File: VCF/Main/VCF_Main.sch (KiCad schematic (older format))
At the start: 56 parts, among them J1 Power, J2 Power, U1 TL072, U2 TL072, U3 AS3320, U4 TL072

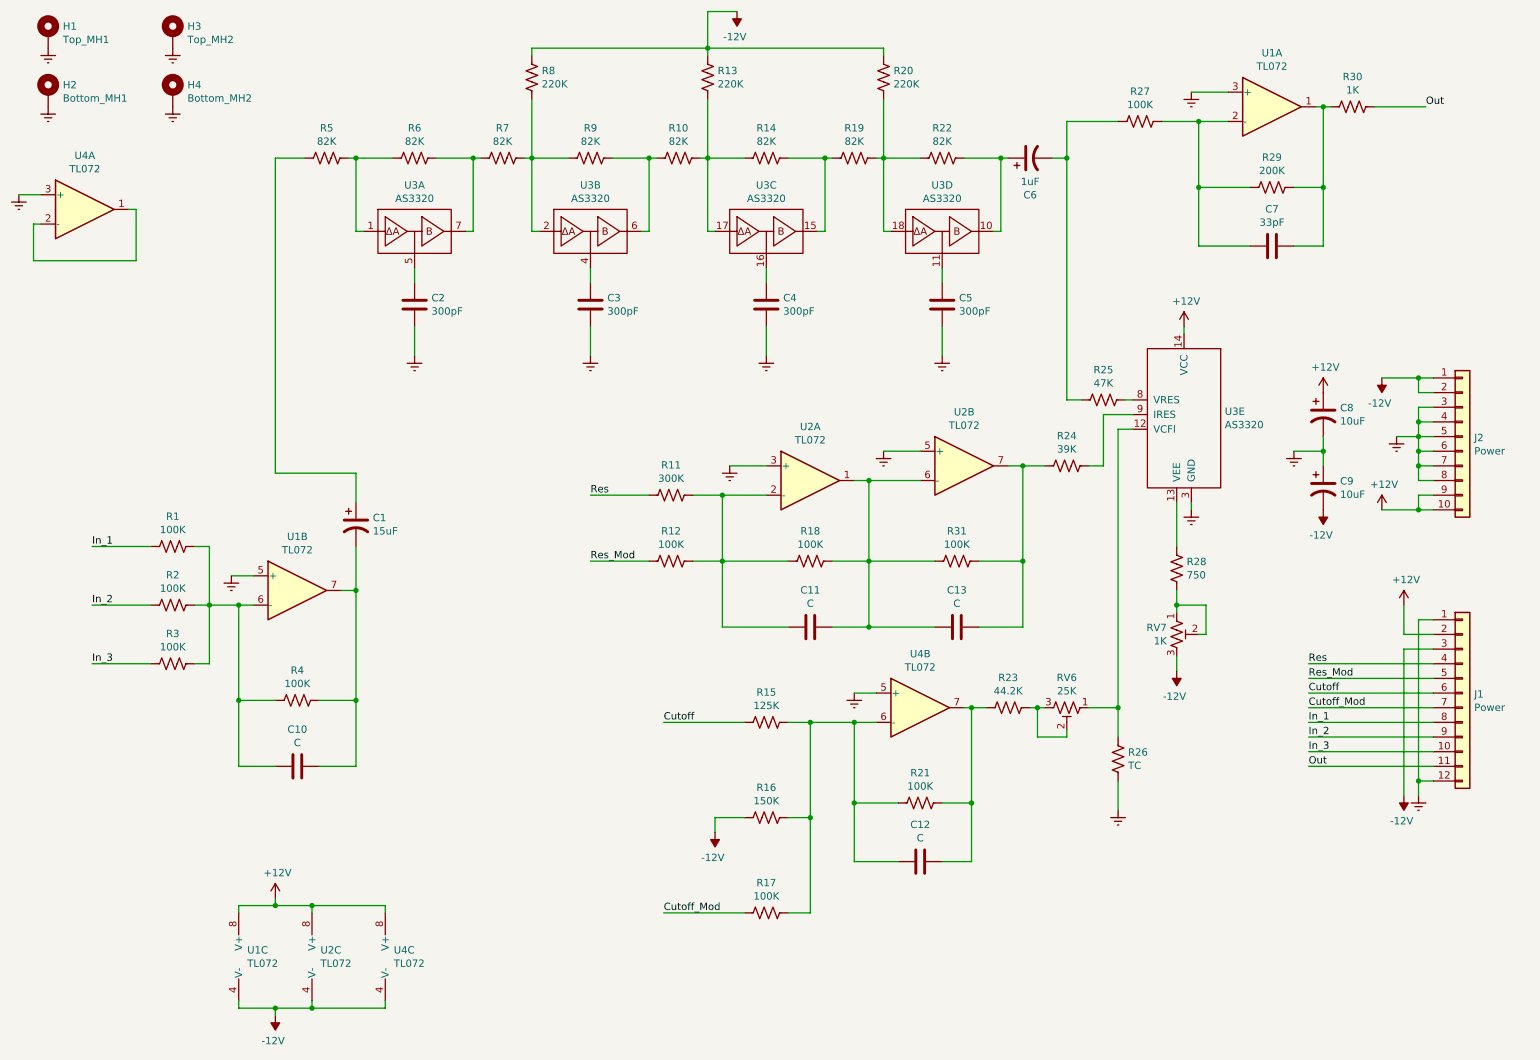
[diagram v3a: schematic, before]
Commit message: Clean up layout of VCF board
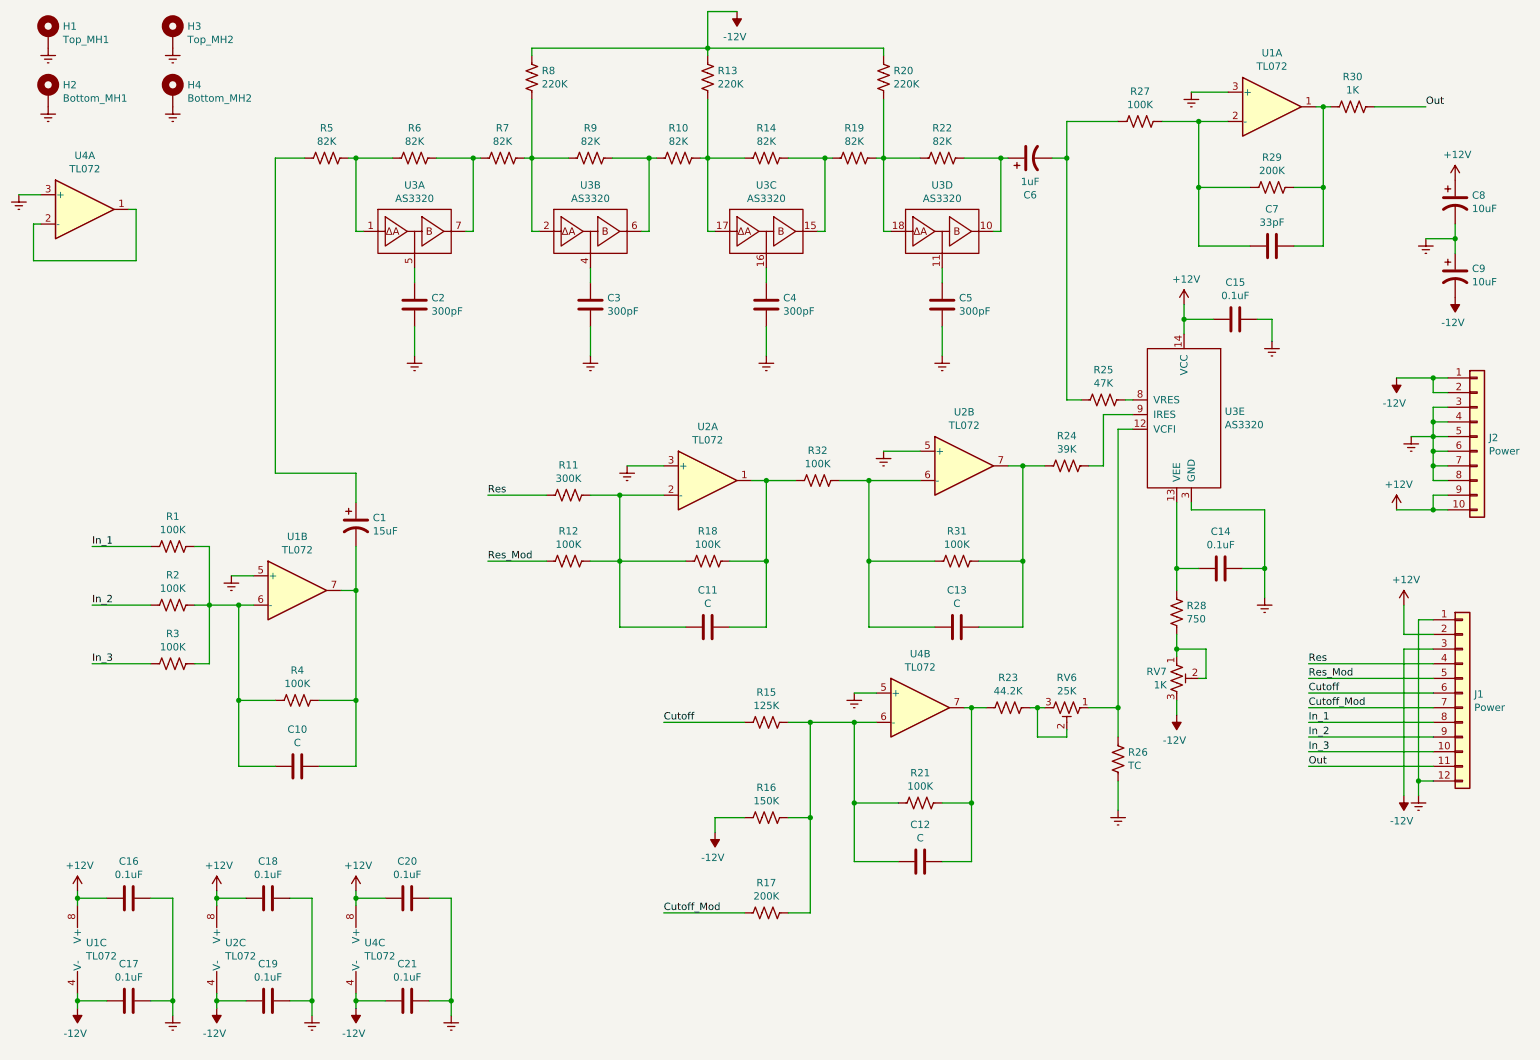
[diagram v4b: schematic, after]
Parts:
- added C14, C15, C16, C17, C18, C19, C20, C21: 0.1uF, Capacitor_SMD:C_0805_2012Metric, symbol Device:C
- added R32: 100K, Resistor_SMD:R_0805_2012Metric, symbol Device:R_US
- R17: value 100K -> 200K
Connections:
- net +12V: now also C15.2, C16.2, C18.2, C20.2
- net -12V: now also C17.2, C19.2, C21.2
- net GNDREF: now also C14.1, C15.1, C16.1, C17.1, C18.1, C19.1, C20.1, C21.1
- net at R28.1, U3.13 (VEE): now also C14.2
- net at C11.2, R18.1, U2.1: now also R32.2; no longer C13.1, R31.2, U2.6 (-)
- new net: C13.1, R31.2, R32.1, U2.6 (-)
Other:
- moved on the sheet: C11, C8, C9, J2, R11, R12, R18, R28, RV7, U1C, U2A, U2C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
